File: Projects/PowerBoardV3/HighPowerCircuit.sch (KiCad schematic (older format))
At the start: 38 parts

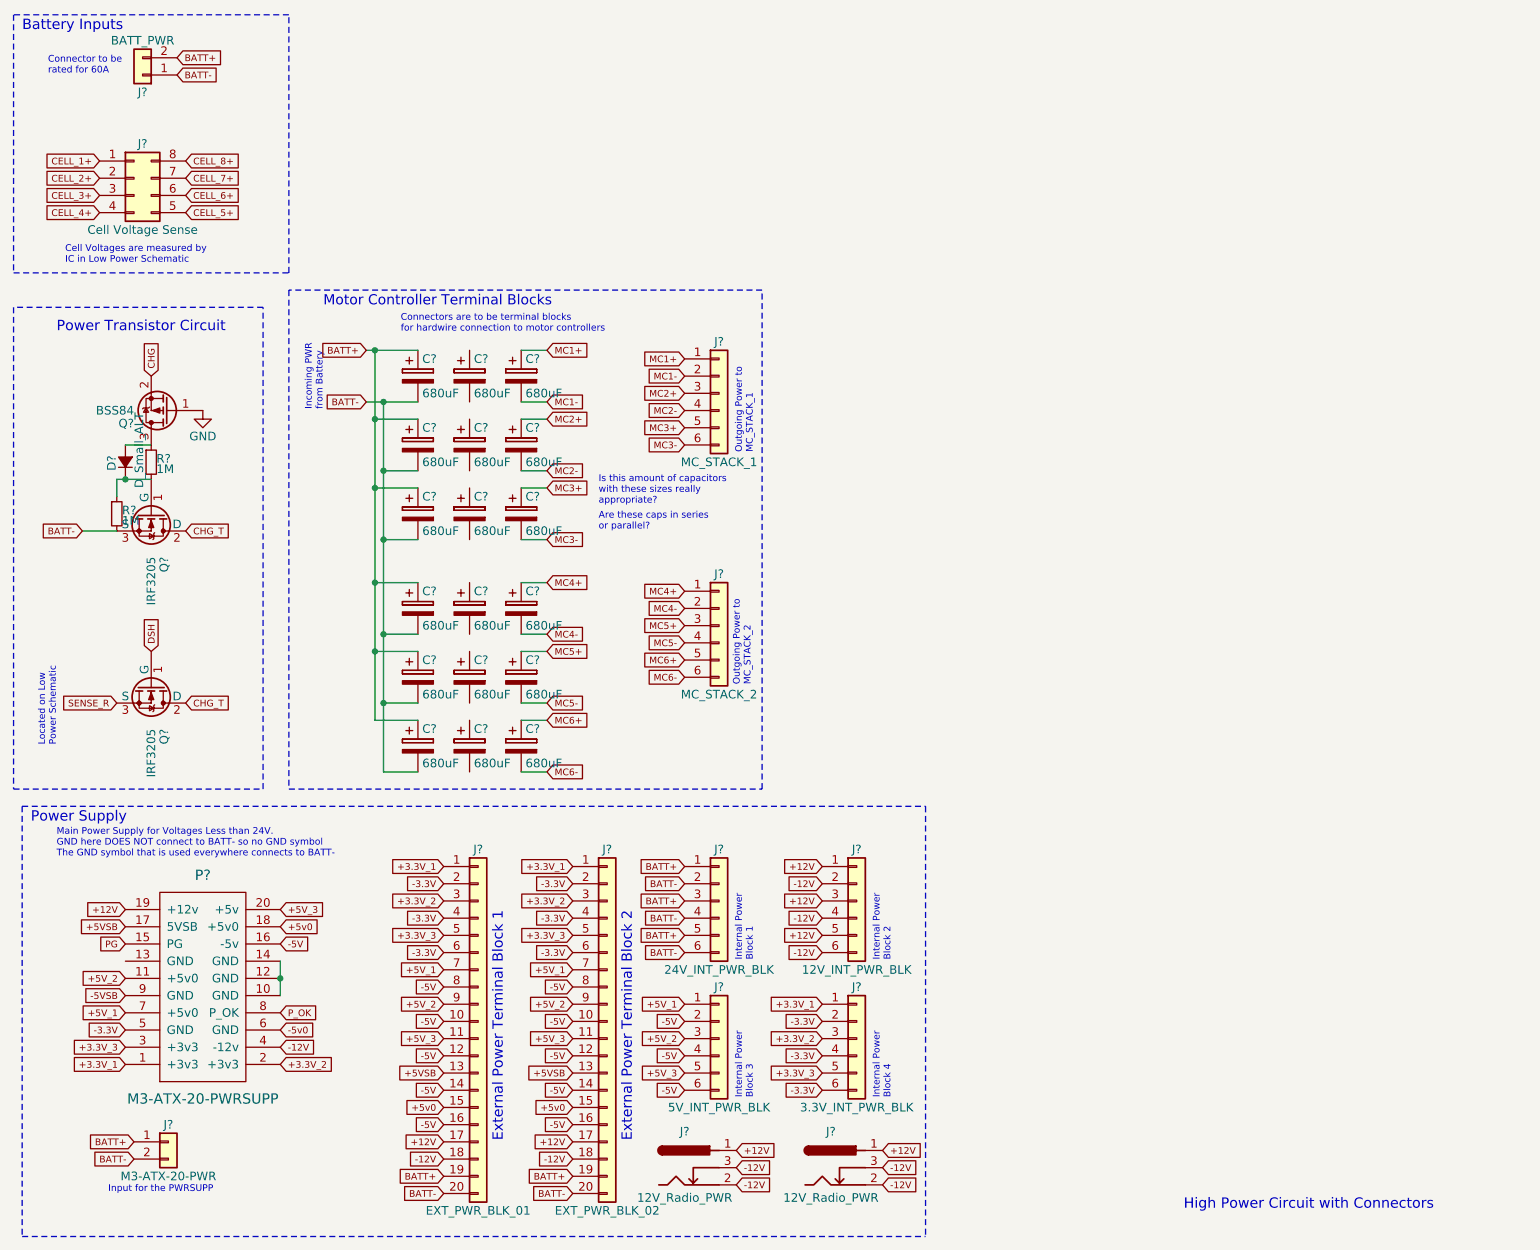
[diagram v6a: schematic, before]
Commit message: Added 9V Power Supply
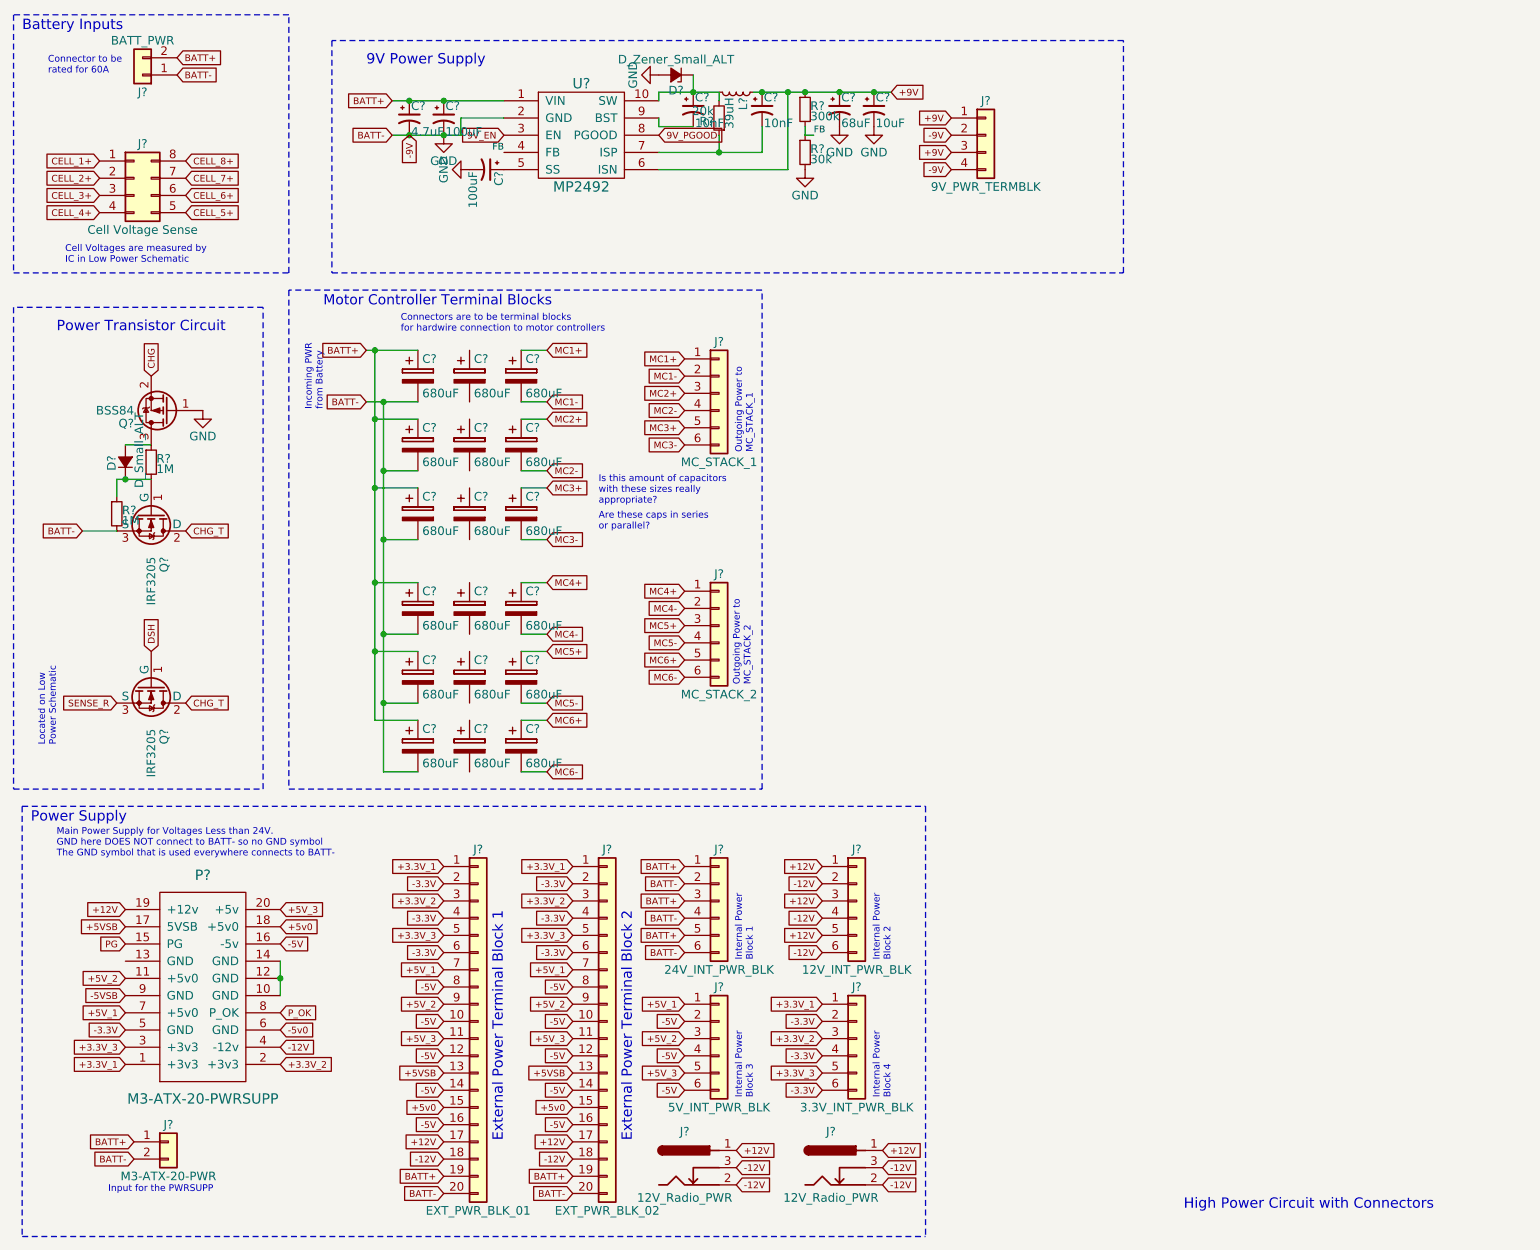
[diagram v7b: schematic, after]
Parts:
- added C? (x2): 100uF, symbol CP1_Small
- added C?: 4.7uF, symbol CP1_Small
- added C? (x2): 10nF, symbol CP1_Small
- added C?: 68uF, symbol CP1_Small
- added C?: 10uF, symbol CP1_Small
- added D?: D_Zener_Small_ALT, symbol D_Zener_Small_ALT
- added J?: 9V_PWR_TERMBLK, symbol Conn_01x04
- added L?: 39uH, symbol L_Small
- added R?: 20k, symbol R_Small
- added R?: 300k, symbol R_Small
- added R?: 30k, symbol R_Small
- added U?: MP2492, symbol MP2492
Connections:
- net BATT- is gone; now on net GND: C?.2, C?.2, C?.2, C?.2, C?.2, C?.2, J?.1 (Pin_1), J?.2 (Pin_2), J?.2 (Pin_2), J?.20 (Pin_20), J?.20 (Pin_20), J?.4 (Pin_4), J?.6 (Pin_6), Q?.3 (S), R?.2
- net BATT+: now also C?.1, C?.1, U?.1 (VIN)
- net GND: now also C?.2, C?.2, C?.2, C?.2, C?.2, D?.2 (A), J?.2 (Pin_2), J?.4 (Pin_4), R?.2, U?.2 (GND)
- new net: C?.1, D?.1 (K), L?.2, R?.2, U?.10 (SW)
- new net: C?.1, U?.5 (SS)
- new net: C?.2, R?.1, U?.7 (ISP)
- new net: C?.2, U?.9 (BST)
- new net +9V: C?.1, C?.1, C?.1, J?.1 (Pin_1), J?.3 (Pin_3), L?.1, R?.1, U?.6 (ISN)
- new net 9V_EN: U?.3 (EN)
- new net 9V_PGOOD: U?.8 (PGOOD)
- new net FB: R?.1, R?.2, U?.4 (FB)
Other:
- note added: "9V Power Supply\n"

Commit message: Changed Global vars to hierarchical
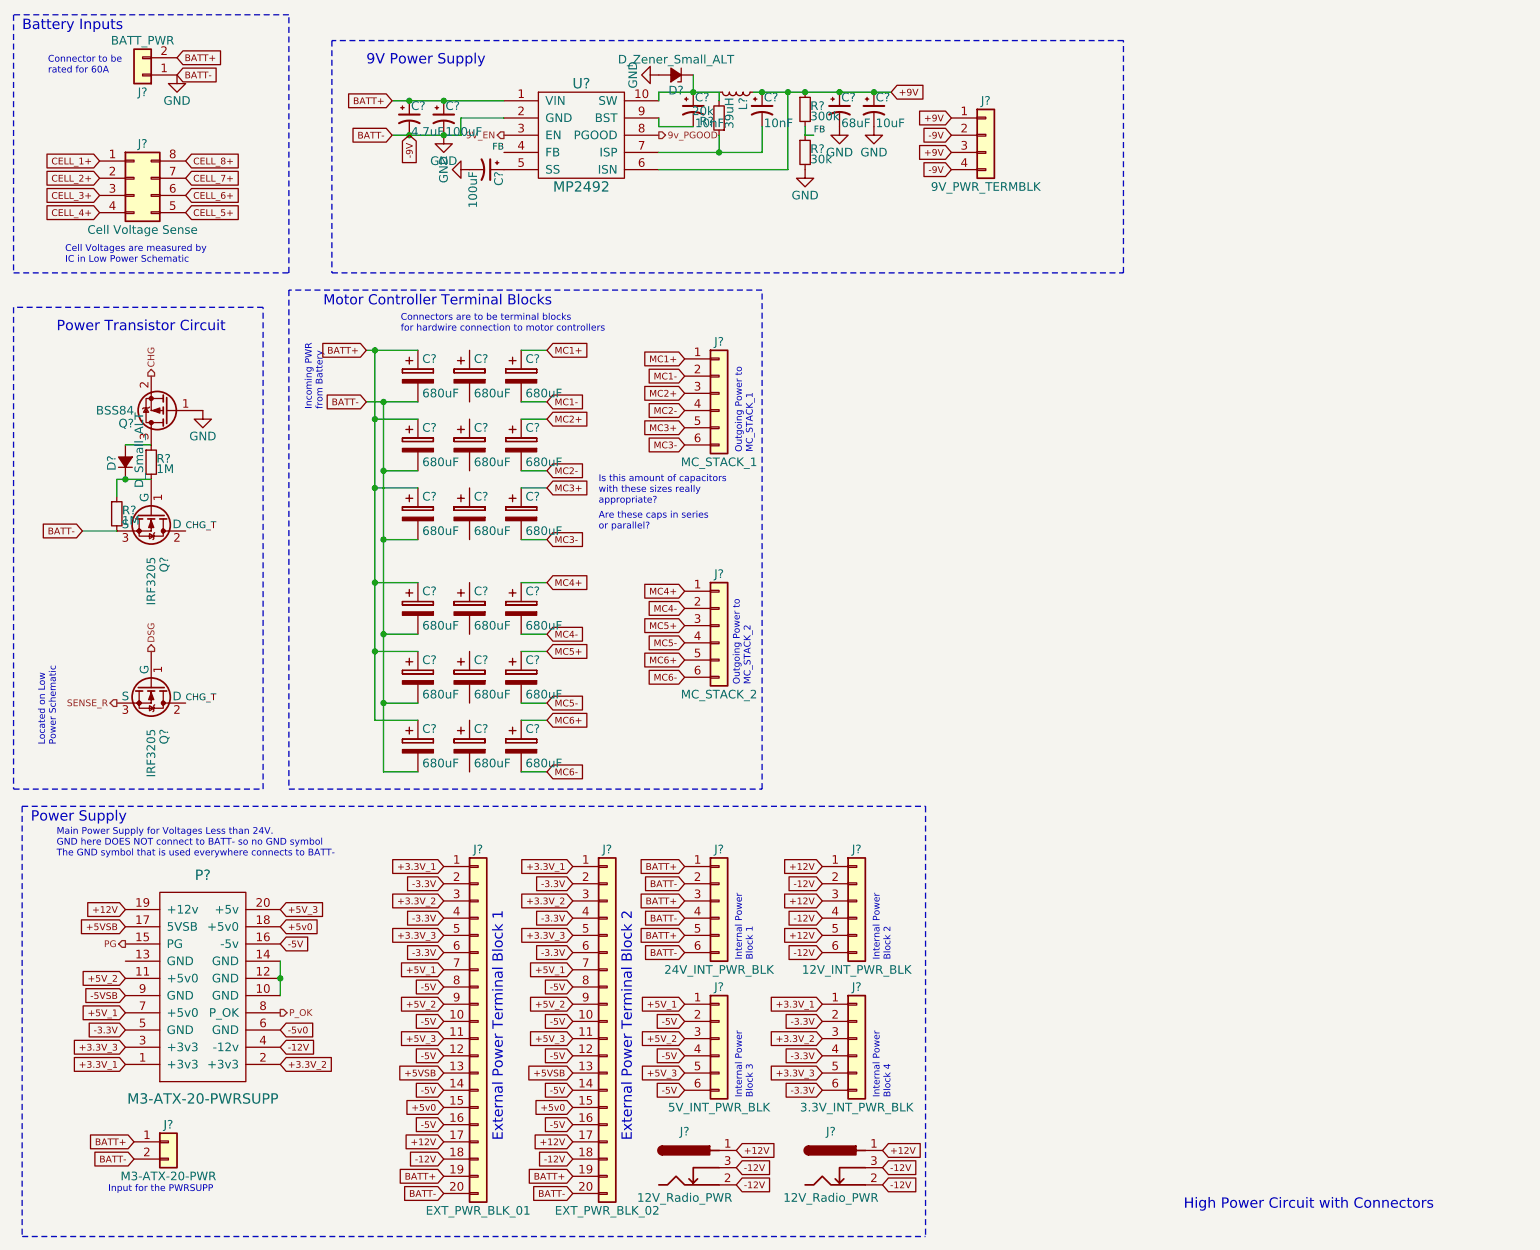
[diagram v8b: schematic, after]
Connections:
- net 9V_PGOOD renamed 9v_PGOOD
- net DSH renamed DSG
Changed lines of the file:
@@
 	0    1    1    0
 $EndComp
-Text GLabel 1350 4250 1    39   Input ~ 0
-DSH
-Text GLabel 1350 2650 1    39   Input ~ 0
-CHG
 $Comp
 L BSS84 Q?
@@
 	1350 3050 1200 3050
 Wire Wire Line
-	1150 3250 1350 3250
+	1150 3250 1200 3250
+Wire Wire Line
+	1200 3250 1350 3250
 $Comp
 L R_Small R?
@@
 Text GLabel 950  3550 0    39   Input ~ 0
 BATT-
-Text GLabel 1550 4550 2    39   Input ~ 0
-CHG_T
-Text GLabel 1550 3550 2    39   Input ~ 0
-CHG_T
-Text GLabel 1150 4550 0    39   Input ~ 0
-SENSE_R
 Text Notes 800  2400 0    60   ~ 0
 Power Transistor Circuit
@@
 Battery Inputs
 Wire Wire Line
-	2100 6050 2100 6250
+	2100 6050 2100 6150
+Wire Wire Line
+	2100 6150 2100 6250
 Connection ~ 2100 6150
 Text GLabel 3050 5500 0    39   Input ~ 0
@@
 Text GLabel 2100 6450 2    39   Input ~ 0
 -5v0
-Text GLabel 1200 5950 0    39   Input ~ 0
-PG
-Text GLabel 2100 6350 2    39   Input ~ 0
-P_OK
 Text GLabel 3050 6800 0    39   Input ~ 0
 -5V
@@
 MC3-
 Wire Wire Line
-	2600 2800 2900 2800
+	2600 2800 2700 2800
+Wire Wire Line
+	2700 2800 2900 2800
 Wire Wire Line
 	2900 3200 2700 3200
@@
 	2700 3600 2900 3600
 Wire Wire Line
-	2700 2800 2700 4950
+	2700 2800 2700 3200
+Wire Wire Line
+	2700 3200 2700 3600
+Wire Wire Line
+	2700 3600 2700 4150
+Wire Wire Line
+	2700 4150 2700 4550
+Wire Wire Line
+	2700 4550 2700 4950
 Connection ~ 2700 3200
 Wire Wire Line
 	2900 2900 2650 2900
 Wire Wire Line
-	2600 2500 2900 2500
+	2600 2500 2650 2500
+Wire Wire Line
+	2650 2500 2900 2500
 Wire Wire Line
 	2650 3300 2900 3300
 Wire Wire Line
-	2650 2500 2650 4650
+	2650 2500 2650 2900
+Wire Wire Line
+	2650 2900 2650 3300
+Wire Wire Line
+	2650 3300 2650 3850
+Wire Wire Line
+	2650 3850 2650 4250
+Wire Wire Line
+	2650 4250 2650 4650
 Connection ~ 2650 2900
 Connection ~ 2700 2800
@@
 $EndComp
 Wire Wire Line
-	2750 1050 3400 1050
+	2750 1050 2850 1050
+Wire Wire Line
+	2850 1050 3050 1050
+Wire Wire Line
+	3050 1050 3400 1050
 Connection ~ 3050 1050
 Connection ~ 2850 1050
@@
 BATT+
 Wire Wire Line
-	2750 1250 3150 1250
+	2750 1250 2850 1250
+Wire Wire Line
+	2850 1250 3050 1250
+Wire Wire Line
+	3050 1250 3150 1250
 Connection ~ 2850 1250
 Text GLabel 2750 1250 0    39   Input ~ 0
@@
 	4300 1050 4300 1000
 Wire Wire Line
-	4300 1000 4650 1000
+	4300 1000 4500 1000
+Wire Wire Line
+	4500 1000 4650 1000
 Wire Wire Line
 	4300 1150 4300 1200
@@
 $EndComp
 Wire Wire Line
-	4300 1350 4900 1350
+	4300 1350 4650 1350
+Wire Wire Line
+	4650 1350 4900 1350
 Connection ~ 4500 1000
 $Comp
@@
 Wire Wire Line
 	4650 1250 4650 1350
-Text GLabel 3400 1250 0    39   Input ~ 0
-9V_EN
-Text GLabel 4300 1250 2    39   Input ~ 0
-9V_PGOOD
 Connection ~ 4900 1000
 Text GLabel 5650 1000 2    39   Input ~ 0
@@
 FB
 Wire Wire Line
-	4850 1000 5650 1000
+	4850 1000 4900 1000
+Wire Wire Line
+	4900 1000 5050 1000
+Wire Wire Line
+	5050 1000 5150 1000
+Wire Wire Line
+	5150 1000 5350 1000
+Wire Wire Line
+	5350 1000 5550 1000
+Wire Wire Line
+	5550 1000 5650 1000
 Text Notes 2600 850  0    60   ~ 0
 9V Power Supply\n
@@
 Wire Wire Line
 	4500 900  4500 1000
+$Comp
+L GND #PWR?
+U 1 1 5AA43AC5
+P 1500 900
+F 0 "#PWR?" H 1500 650 50  0001 C CNN
+F 1 "GND" H 1500 750 50  0000 C CNN
+F 2 "" H 1500 900 50  0001 C CNN
+F 3 "" H 1500 900 50  0001 C CNN
+	1    1500 900
+	1    0    0    -1
+$EndComp
+Text Label 1550 3550 0    39   ~ 0
+CHG_T
+Text Label 1550 4550 0    39   ~ 0
+CHG_T
+Text HLabel 1150 4550 0    39   Output ~ 0
+SENSE_R
+Text HLabel 1350 2650 1    39   Output ~ 0
+CHG
+Text HLabel 1350 4250 1    39   Output ~ 0
+DSG
+Text HLabel 2100 6350 2    39   Output ~ 0
+P_OK
+Text HLabel 1200 5950 0    39   Output ~ 0
+PG
+Text HLabel 3400 1250 0    39   Output ~ 0
+9V_EN
+Text HLabel 4300 1250 2    39   Output ~ 0
+9v_PGOOD
 $EndSCHEMATC
